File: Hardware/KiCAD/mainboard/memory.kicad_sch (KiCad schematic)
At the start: 8 parts, among them J6 Micro_SD_Card_Det

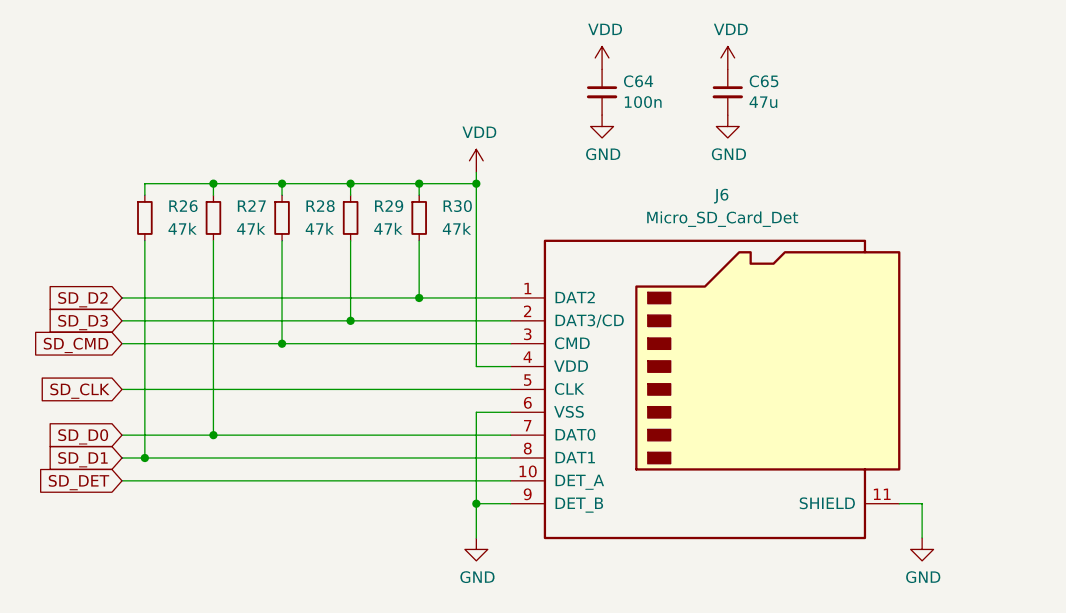
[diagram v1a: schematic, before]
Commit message: MCU swap
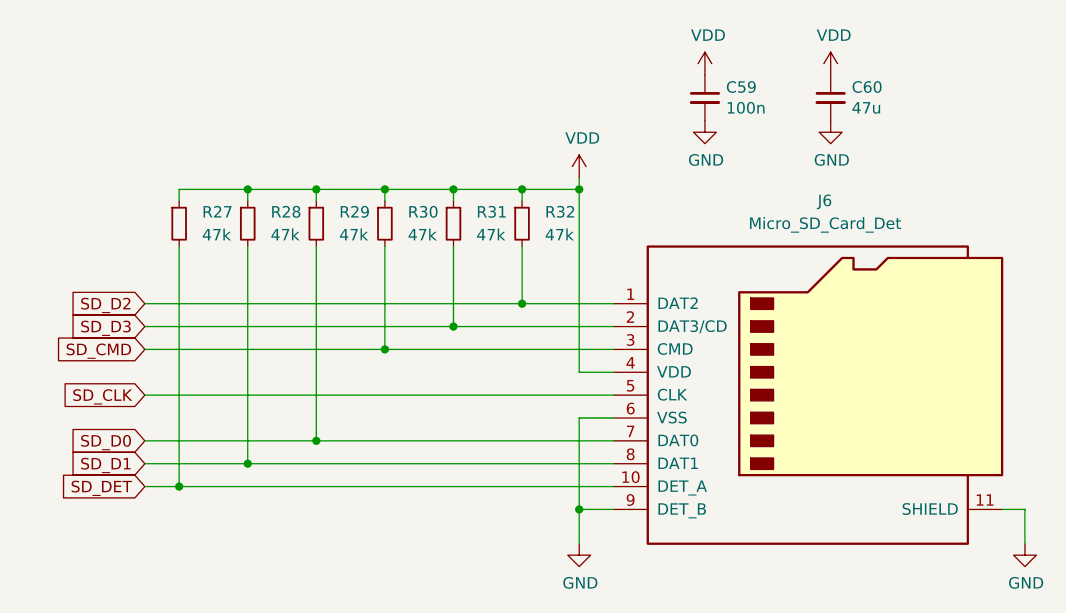
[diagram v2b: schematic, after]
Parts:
- added R27: 47k, Resistor_SMD:R_0402_1005Metric, symbol Device:R_Small
- renumbered C64 to C59, C65 to C60, R26 to R28, R27 to R29, R28 to R30, R29 to R31, R30 to R32
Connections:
- net SD_DET: now also R27.2
- net VDD: now also R27.1
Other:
- moved on the sheet: C59, C60, J6, R28, R29, R30, R31, R32

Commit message: Removed RTC
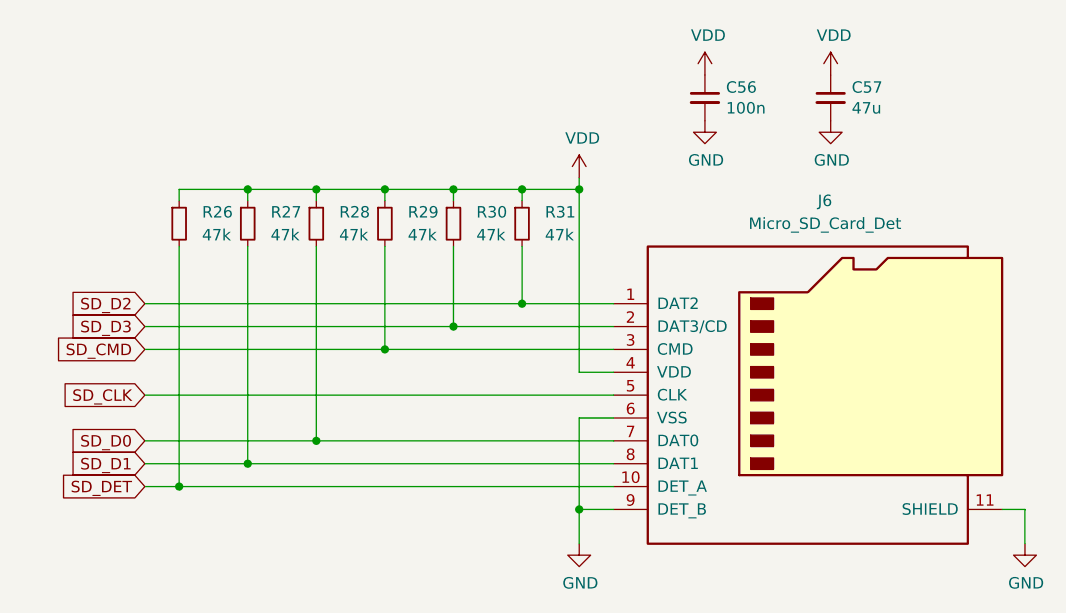
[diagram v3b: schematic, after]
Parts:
- renumbered C59 to C56, C60 to C57, R27 to R26, R28 to R27, R29 to R28, R30 to R29, R31 to R30, R32 to R31
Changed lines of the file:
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@@
   (symbol (lib_id "power:GND") (at 173.99 71.12 0) (unit 1)
     (in_bom yes) (on_board yes)
-    (property "Reference" "#PWR0117" (id 0) (at 173.99 77.47 0)
+    (property "Reference" "#PWR0111" (id 0) (at 173.99 77.47 0)
       (effects (font (size 1.27 1.27)) hide)
     )
@@
   (symbol (lib_id "power:VDD") (at 173.99 66.04 0) (unit 1)
     (in_bom yes) (on_board yes)
-    (property "Reference" "#PWR0116" (id 0) (at 173.99 69.85 0)
+    (property "Reference" "#PWR0110" (id 0) (at 173.99 69.85 0)
       (effects (font (size 1.27 1.27)) hide)
     )
@@
   (symbol (lib_id "Device:R_Small") (at 124.46 82.55 0) (unit 1)
     (in_bom yes) (on_board yes) (fields_autoplaced)
-    (property "Reference" "R30" (id 0) (at 127 81.2799 0)
+    (property "Reference" "R29" (id 0) (at 127 81.2799 0)
       (effects (font (size 1.27 1.27)) (justify left))
     )
@@
   (symbol (lib_id "Device:R_Small") (at 139.7 82.55 0) (unit 1)
     (in_bom yes) (on_board yes) (fields_autoplaced)
-    (property "Reference" "R32" (id 0) (at 142.24 81.2799 0)
+    (property "Reference" "R31" (id 0) (at 142.24 81.2799 0)
       (effects (font (size 1.27 1.27)) (justify left))
     )
@@
   (symbol (lib_id "power:VDD") (at 146.05 77.47 0) (unit 1)
     (in_bom yes) (on_board yes)
-    (property "Reference" "#PWR0112" (id 0) (at 146.05 81.28 0)
+    (property "Reference" "#PWR0106" (id 0) (at 146.05 81.28 0)
       (effects (font (size 1.27 1.27)) hide)
     )
@@
   (symbol (lib_id "power:GND") (at 160.02 71.12 0) (unit 1)
     (in_bom yes) (on_board yes)
-    (property "Reference" "#PWR0115" (id 0) (at 160.02 77.47 0)
+    (property "Reference" "#PWR0109" (id 0) (at 160.02 77.47 0)
       (effects (font (size 1.27 1.27)) hide)
     )
@@
   (symbol (lib_id "power:VDD") (at 160.02 66.04 0) (unit 1)
     (in_bom yes) (on_board yes)
-    (property "Reference" "#PWR0114" (id 0) (at 160.02 69.85 0)
+    (property "Reference" "#PWR0108" (id 0) (at 160.02 69.85 0)
       (effects (font (size 1.27 1.27)) hide)
     )
@@
   (symbol (lib_id "power:GND") (at 195.58 118.11 0) (unit 1)
     (in_bom yes) (on_board yes)
-    (property "Reference" "#PWR0118" (id 0) (at 195.58 124.46 0)
+    (property "Reference" "#PWR0112" (id 0) (at 195.58 124.46 0)
       (effects (font (size 1.27 1.27)) hide)
     )
@@
   (symbol (lib_id "pkl_device:pkl_C_Small") (at 160.02 68.58 0) (unit 1)
     (in_bom no) (on_board no)
-    (property "Reference" "C59" (id 0) (at 162.3568 67.4116 0)
+    (property "Reference" "C56" (id 0) (at 162.3568 67.4116 0)
       (effects (font (size 1.27 1.27)) (justify left))
     )
@@
   (symbol (lib_id "Device:R_Small") (at 109.22 82.55 0) (unit 1)
     (in_bom yes) (on_board yes) (fields_autoplaced)
-    (property "Reference" "R28" (id 0) (at 111.76 81.2799 0)
+    (property "Reference" "R27" (id 0) (at 111.76 81.2799 0)
       (effects (font (size 1.27 1.27)) (justify left))
     )
@@
   (symbol (lib_id "Device:R_Small") (at 116.84 82.55 0) (unit 1)
     (in_bom yes) (on_board yes) (fields_autoplaced)
-    (property "Reference" "R29" (id 0) (at 119.38 81.2799 0)
+    (property "Reference" "R28" (id 0) (at 119.38 81.2799 0)
       (effects (font (size 1.27 1.27)) (justify left))
     )
@@
   (symbol (lib_id "pkl_device:pkl_C_Small") (at 173.99 68.58 0) (unit 1)
     (in_bom no) (on_board no)
-    (property "Reference" "C60" (id 0) (at 176.3268 67.4116 0)
+    (property "Reference" "C57" (id 0) (at 176.3268 67.4116 0)
       (effects (font (size 1.27 1.27)) (justify left))
     )
@@
   (symbol (lib_id "Device:R_Small") (at 101.6 82.55 0) (unit 1)
     (in_bom yes) (on_board yes) (fields_autoplaced)
-    (property "Reference" "R27" (id 0) (at 104.14 81.2799 0)
+    (property "Reference" "R26" (id 0) (at 104.14 81.2799 0)
       (effects (font (size 1.27 1.27)) (justify left))
     )
@@
   (symbol (lib_id "Device:R_Small") (at 132.08 82.55 0) (unit 1)
     (in_bom yes) (on_board yes) (fields_autoplaced)
-    (property "Reference" "R31" (id 0) (at 134.62 81.2799 0)
+    (property "Reference" "R30" (id 0) (at 134.62 81.2799 0)
       (effects (font (size 1.27 1.27)) (justify left))
     )
@@
   (symbol (lib_id "power:GND") (at 146.05 118.11 0) (unit 1)
     (in_bom yes) (on_board yes)
-    (property "Reference" "#PWR0113" (id 0) (at 146.05 124.46 0)
-      (effects (font (size 1.27 1.27)) hide)
-    )
+    (property "Reference" "#PWR0107" (id 0) (at 146.05 124.46 0)
+      (effects (font (size 1.27 1.27)) hide)
+    )
